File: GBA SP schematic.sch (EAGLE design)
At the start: 187 parts, among them IC2 FT230XQ, J1 DNP, J11 Debug USB, J12 FPC_14, J13 DNP, J14 FPC_14, J2 MICRO_USB, J4 DNP, J5 DNP, J6 FPC_14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

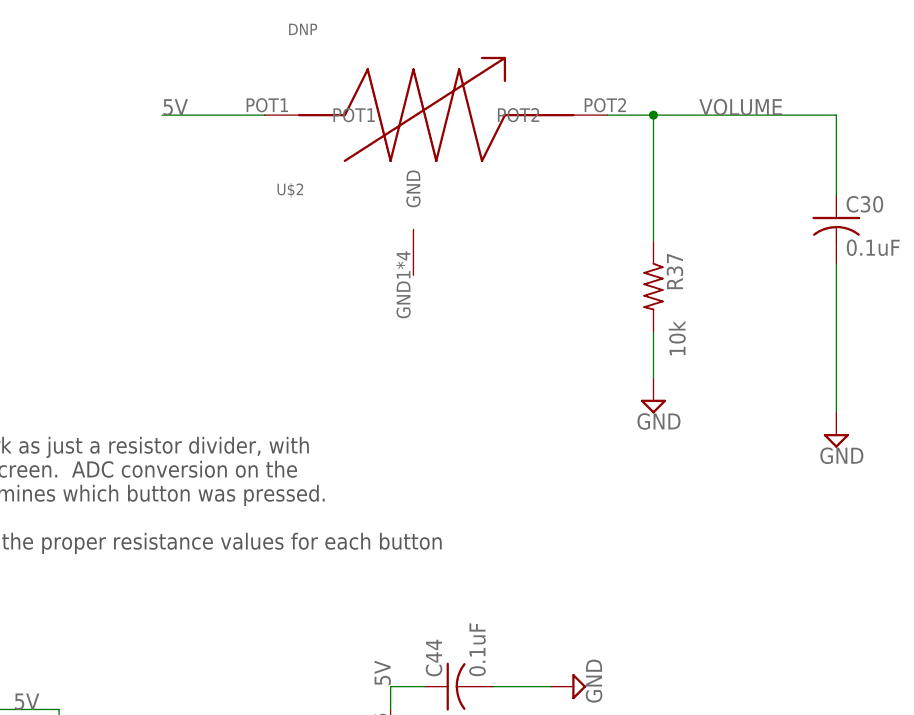
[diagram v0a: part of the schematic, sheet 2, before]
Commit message: mounting holes, fixed volume circuit
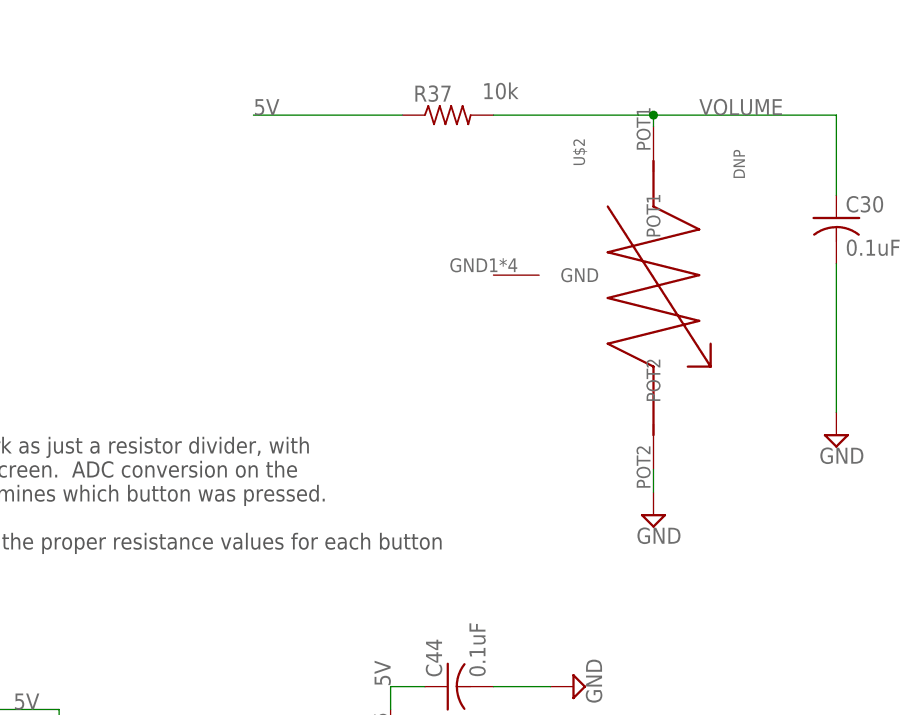
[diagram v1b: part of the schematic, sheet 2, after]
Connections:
- net 5V: now also R37.1; no longer U$2.POT1
- net GND: now also U$2.POT2; no longer R37.2
- net VOLUME: now also R37.2, U$2.POT1; no longer R37.1, U$2.POT2
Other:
- moved on the sheet: R37, U$2
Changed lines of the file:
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@@
 <attribute name="MPN" x="71.12" y="36.83" size="1.778" layer="96" rot="R90" display="off"/>
 </instance>
-<instance part="U$2" gate="G$1" x="210.82" y="203.2"/>
+<instance part="U$2" gate="G$1" x="237.49" y="185.42" rot="R270"/>
 <instance part="SW_L" gate="G$1" x="31.75" y="196.85" smashed="yes">
 <attribute name="NAME" x="26.162" y="201.676" size="1.778" layer="95"/>
@@
 <instance part="SUPPLY30" gate="GND" x="59.69" y="186.69"/>
 <instance part="SUPPLY78" gate="GND" x="257.81" y="167.64"/>
-<instance part="SUPPLY79" gate="GND" x="237.49" y="171.45"/>
+<instance part="SUPPLY79" gate="GND" x="237.49" y="158.75"/>
 <instance part="C30" gate="G$1" x="257.81" y="191.77">
 <attribute name="DIGIKEY" x="257.81" y="191.77" size="1.778" layer="96" display="off"/>
@@
 <attribute name="MPN" x="257.81" y="191.77" size="1.778" layer="96" display="off"/>
 </instance>
-<instance part="R37" gate="G$1" x="237.49" y="184.15" smashed="yes" rot="R270">
-<attribute name="NAME" x="238.9886" y="187.96" size="1.778" layer="95" rot="R270"/>
-<attribute name="VALUE" x="239.268" y="180.34" size="1.778" layer="96" rot="R270"/>
+<instance part="R37" gate="G$1" x="214.63" y="203.2" smashed="yes">
+<attribute name="NAME" x="210.82" y="204.6986" size="1.778" layer="95"/>
+<attribute name="VALUE" x="218.44" y="204.978" size="1.778" layer="96"/>
 </instance>
 <instance part="C31" gate="G$1" x="25.4" y="130.81">
@@
 </segment>
 <segment>
-<pinref part="R37" gate="G$1" pin="2"/>
-<wire x1="237.49" y1="179.07" x2="237.49" y2="173.99" width="0.1524" layer="91"/>
+<pinref part="U$2" gate="G$1" pin="POT2"/>
 <pinref part="SUPPLY79" gate="GND" pin="GND"/>
+<wire x1="237.49" y1="163.83" x2="237.49" y2="161.29" width="0.1524" layer="91"/>
 </segment>
 </net>
@@
 <wire x1="257.81" y1="203.2" x2="237.49" y2="203.2" width="0.1524" layer="91"/>
 <label x="242.57" y="203.2" size="1.778" layer="95"/>
-<pinref part="U$2" gate="G$1" pin="POT2"/>
-<pinref part="R37" gate="G$1" pin="1"/>
-<wire x1="237.49" y1="203.2" x2="232.41" y2="203.2" width="0.1524" layer="91"/>
-<wire x1="237.49" y1="203.2" x2="237.49" y2="189.23" width="0.1524" layer="91"/>
+<pinref part="U$2" gate="G$1" pin="POT1"/>
+<wire x1="237.49" y1="201.93" x2="237.49" y2="203.2" width="0.1524" layer="91"/>
+<pinref part="R37" gate="G$1" pin="2"/>
+<wire x1="237.49" y1="203.2" x2="219.71" y2="203.2" width="0.1524" layer="91"/>
 <junction x="237.49" y="203.2"/>
 </segment>
@@
 </segment>
 <segment>
-<pinref part="U$2" gate="G$1" pin="POT1"/>
-<wire x1="194.31" y1="203.2" x2="182.88" y2="203.2" width="0.1524" layer="91"/>
-<label x="182.88" y="203.2" size="1.778" layer="95"/>
+<pinref part="R37" gate="G$1" pin="1"/>
+<wire x1="209.55" y1="203.2" x2="193.04" y2="203.2" width="0.1524" layer="91"/>
+<label x="193.04" y="203.2" size="1.778" layer="95"/>
 </segment>
 </net>
